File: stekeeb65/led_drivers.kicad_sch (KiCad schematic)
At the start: 28 parts

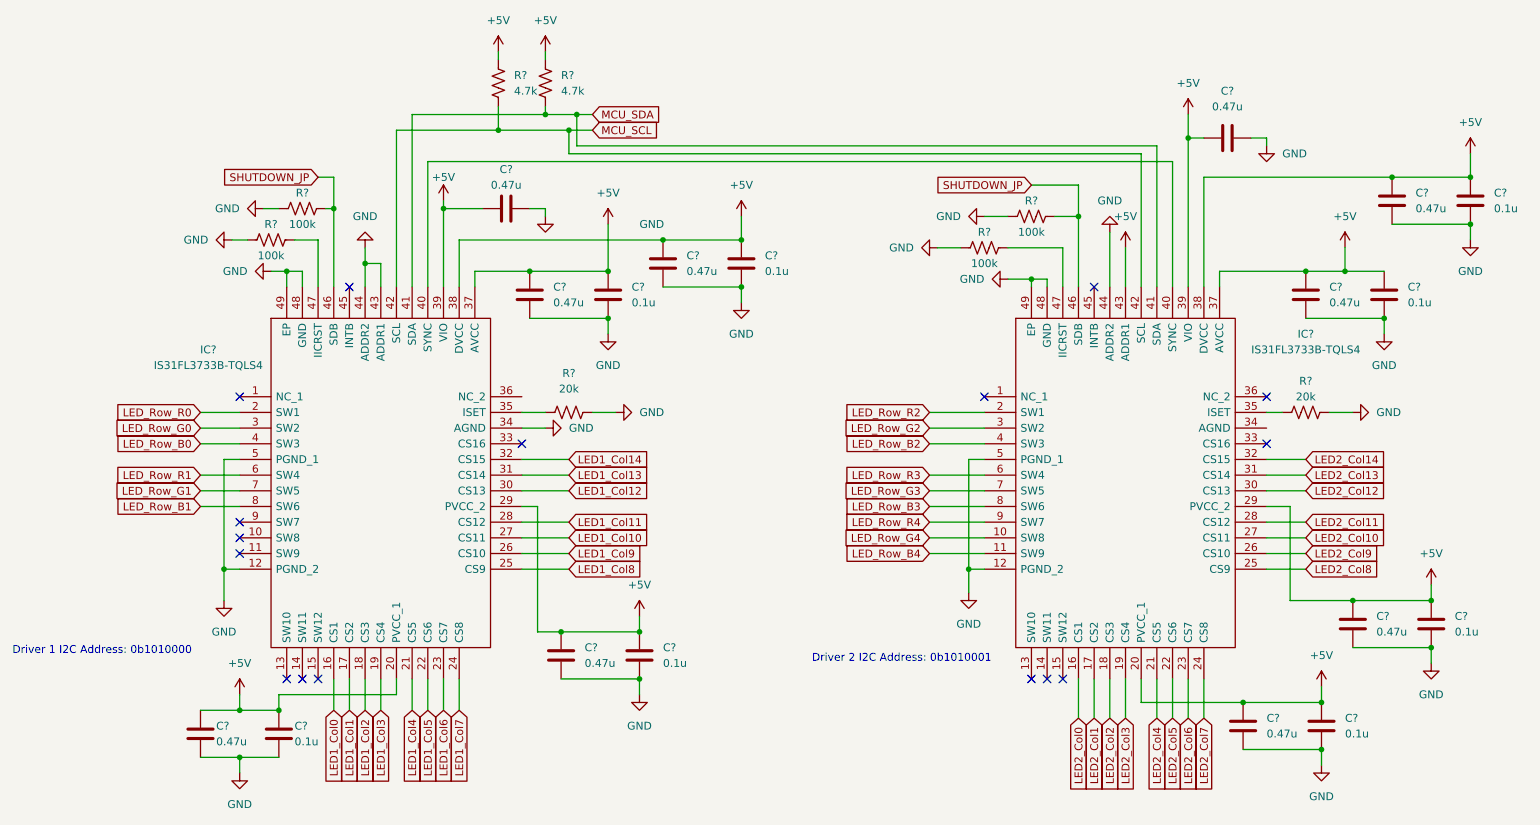
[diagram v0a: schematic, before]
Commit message: Adding keyboard footprints
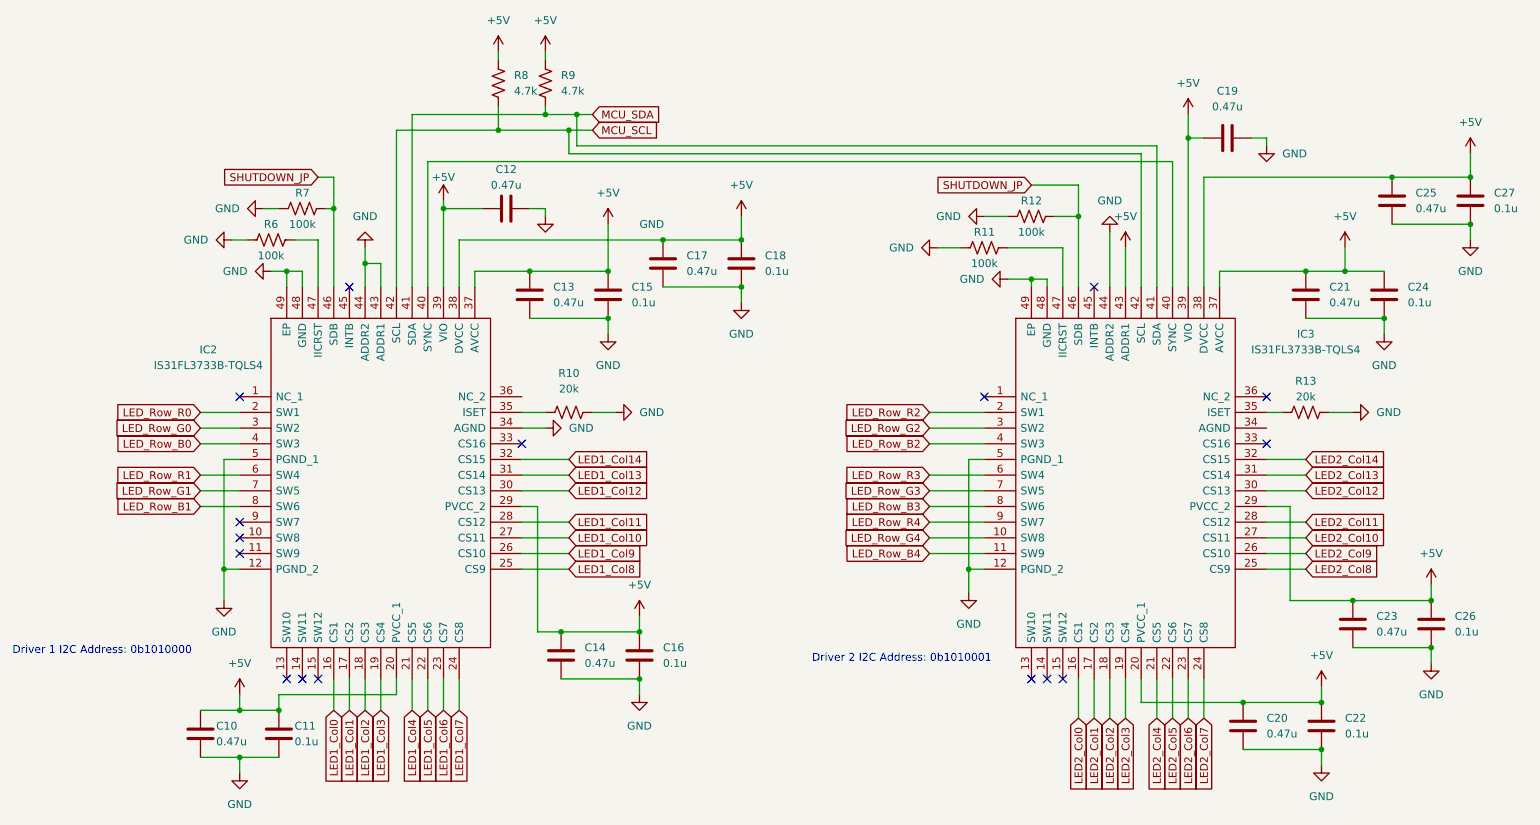
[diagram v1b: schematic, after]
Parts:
- C10, C11, C12, C13, C14, C15, C16, C17, C18, C19, C20, C21, C22, C23, C24, C25, C26, C27: renamed from C?; footprint (none) -> Capacitor_SMD:C_0805_2012Metric_Pad1.18x1.45mm_HandSolder
- R10, R11, R12, R13, R6, R7, R8, R9: renamed from R?; footprint (none) -> Resistor_SMD:R_0805_2012Metric_Pad1.20x1.40mm_HandSolder
- gave numbers to parts that had none: 2

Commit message: Adding key layout with leds
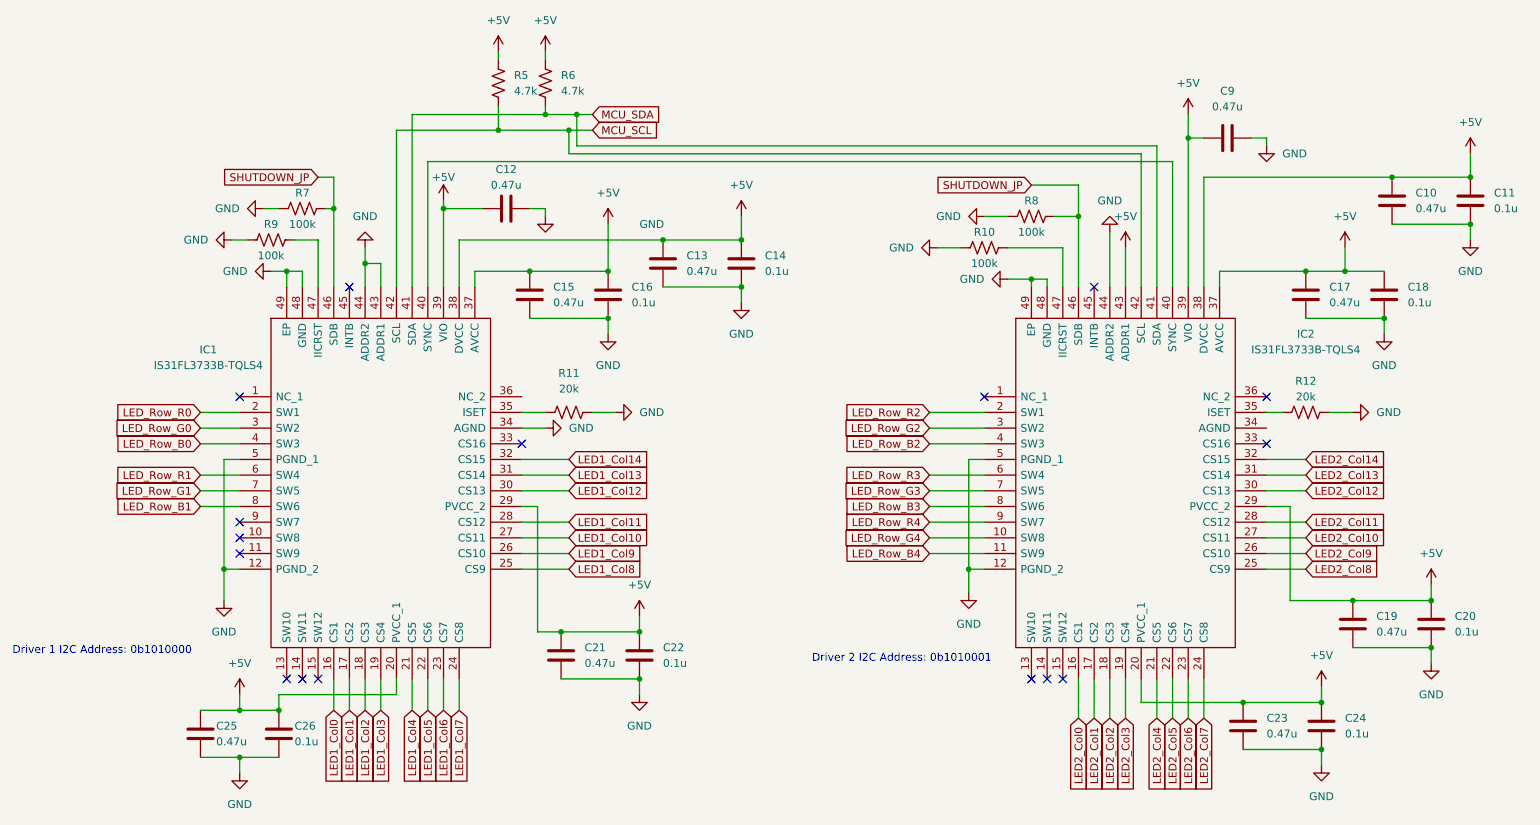
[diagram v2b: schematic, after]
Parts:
- renumbered C25 to C10, C27 to C11, C17 to C13, C18 to C14, C13 to C15, C15 to C16, C21 to C17, C24 to C18, C23 to C19, C26 to C20, C14 to C21, C16 to C22, C20 to C23, C22 to C24, C10 to C25, C11 to C26, C19 to C9, IC2 to IC1, IC3 to IC2, R11 to R10, R10 to R11, R13 to R12, R8 to R5, R9 to R6, R12 to R8, R6 to R9

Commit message: Adding layout for diodes, LEDs, edge cuts
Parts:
- IC1, IC2: footprint QFP50P900X900X120-49N -> SamacSys_Parts:QFP50P900X900X120-49N
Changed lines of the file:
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@@
     (property "Reference" "IC2" (id 0) (at 231.14 66.04 0))
     (property "Value" "IS31FL3733B-TQLS4" (id 1) (at 231.14 68.58 0))
-    (property "Footprint" "QFP50P900X900X120-49N" (id 2) (at 220.98 63.5 0)
+    (property "Footprint" "SamacSys_Parts:QFP50P900X900X120-49N" (id 2) (at 220.98 63.5 0)
       (effects (font (size 1.27 1.27)) (justify left) hide)
     )
@@
     (property "Reference" "IC1" (id 0) (at 53.34 68.58 0))
     (property "Value" "IS31FL3733B-TQLS4" (id 1) (at 53.34 71.12 0))
-    (property "Footprint" "QFP50P900X900X120-49N" (id 2) (at 100.33 63.5 0)
-      (effects (font (size 1.27 1.27)) (justify left) hide)
-    )
+    (property "Footprint" "SamacSys_Parts:QFP50P900X900X120-49N" (id 2) (at 100.33 63.5 0)
+      (effects (font (size 1.27 1.27)) (justify left) hide)
+    )

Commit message: Started layout for keyboard. still need to verify LED driver schematic
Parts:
- C10, C11, C12, C13, C14, C15, C16, C17, C18, C19, C20, C21, C22, C23, C24, C25, C26, C9: footprint Capacitor_SMD:C_0805_2012Metric_Pad1.18x1.45mm_HandSolder -> Capacitor_SMD:C_0603_1608Metric_Pad1.08x0.95mm_HandSolder
- R10, R11, R12, R5, R6, R7, R8, R9: footprint Resistor_SMD:R_0805_2012Metric_Pad1.20x1.40mm_HandSolder -> Resistor_SMD:R_0603_1608Metric_Pad0.98x0.95mm_HandSolder
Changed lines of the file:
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@@
       (effects (font (size 1.27 1.27)) (justify left))
     )
-    (property "Footprint" "Capacitor_SMD:C_0805_2012Metric_Pad1.18x1.45mm_HandSolder" (id 2) (at 252.4252 116.84 0)
+    (property "Footprint" "Capacitor_SMD:C_0603_1608Metric_Pad1.08x0.95mm_HandSolder" (id 2) (at 252.4252 116.84 0)
       (effects (font (size 1.27 1.27)) hide)
     )
@@
       (effects (font (size 1.27 1.27)) (justify left))
     )
-    (property "Footprint" "Capacitor_SMD:C_0805_2012Metric_Pad1.18x1.45mm_HandSolder" (id 2) (at 53.0352 134.62 0)
+    (property "Footprint" "Capacitor_SMD:C_0603_1608Metric_Pad1.08x0.95mm_HandSolder" (id 2) (at 53.0352 134.62 0)
       (effects (font (size 1.27 1.27)) hide)
     )
@@
       (effects (font (size 1.27 1.27)) (justify left))
     )
-    (property "Footprint" "Capacitor_SMD:C_0805_2012Metric_Pad1.18x1.45mm_HandSolder" (id 2) (at 119.0752 63.5 0)
+    (property "Footprint" "Capacitor_SMD:C_0603_1608Metric_Pad1.08x0.95mm_HandSolder" (id 2) (at 119.0752 63.5 0)
       (effects (font (size 1.27 1.27)) hide)
     )
@@
       (effects (font (size 1.27 1.27)) (justify left))
     )
-    (property "Footprint" "Capacitor_SMD:C_0805_2012Metric_Pad1.18x1.45mm_HandSolder" (id 2) (at 244.8052 63.5 0)
+    (property "Footprint" "Capacitor_SMD:C_0603_1608Metric_Pad1.08x0.95mm_HandSolder" (id 2) (at 244.8052 63.5 0)
       (effects (font (size 1.27 1.27)) hide)
     )
@@
     (property "Reference" "C9" (id 0) (at 218.44 26.67 90))
     (property "Value" "0.47u" (id 1) (at 218.44 29.21 90))
-    (property "Footprint" "Capacitor_SMD:C_0805_2012Metric_Pad1.18x1.45mm_HandSolder" (id 2) (at 222.25 33.3248 0)
+    (property "Footprint" "Capacitor_SMD:C_0603_1608Metric_Pad1.08x0.95mm_HandSolder" (id 2) (at 222.25 33.3248 0)
       (effects (font (size 1.27 1.27)) hide)
     )
@@
     (property "Reference" "R9" (id 0) (at 63.5 48.26 90))
     (property "Value" "100k" (id 1) (at 63.5 53.34 90))
-    (property "Footprint" "Resistor_SMD:R_0805_2012Metric_Pad1.20x1.40mm_HandSolder" (id 2) (at 63.754 49.784 90)
+    (property "Footprint" "Resistor_SMD:R_0603_1608Metric_Pad0.98x0.95mm_HandSolder" (id 2) (at 63.754 49.784 90)
       (effects (font (size 1.27 1.27)) hide)
     )
@@
       (effects (font (size 1.27 1.27)) (justify left))
     )
-    (property "Footprint" "Capacitor_SMD:C_0805_2012Metric_Pad1.18x1.45mm_HandSolder" (id 2) (at 111.4552 121.92 0)
+    (property "Footprint" "Capacitor_SMD:C_0603_1608Metric_Pad1.08x0.95mm_HandSolder" (id 2) (at 111.4552 121.92 0)
       (effects (font (size 1.27 1.27)) hide)
     )
@@
     (property "Reference" "C12" (id 0) (at 101.6 39.37 90))
     (property "Value" "0.47u" (id 1) (at 101.6 41.91 90))
-    (property "Footprint" "Capacitor_SMD:C_0805_2012Metric_Pad1.18x1.45mm_HandSolder" (id 2) (at 105.41 44.7548 0)
+    (property "Footprint" "Capacitor_SMD:C_0603_1608Metric_Pad1.08x0.95mm_HandSolder" (id 2) (at 105.41 44.7548 0)
       (effects (font (size 1.27 1.27)) hide)
     )
@@
       (effects (font (size 1.27 1.27)) (justify left))
     )
-    (property "Footprint" "Capacitor_SMD:C_0805_2012Metric_Pad1.18x1.45mm_HandSolder" (id 2) (at 127.9652 58.42 0)
+    (property "Footprint" "Capacitor_SMD:C_0603_1608Metric_Pad1.08x0.95mm_HandSolder" (id 2) (at 127.9652 58.42 0)
       (effects (font (size 1.27 1.27)) hide)
     )
@@
       (effects (font (size 1.27 1.27)) (justify left))
     )
-    (property "Footprint" "Capacitor_SMD:C_0805_2012Metric_Pad1.18x1.45mm_HandSolder" (id 2) (at 221.9452 133.35 0)
+    (property "Footprint" "Capacitor_SMD:C_0603_1608Metric_Pad1.08x0.95mm_HandSolder" (id 2) (at 221.9452 133.35 0)
       (effects (font (size 1.27 1.27)) hide)
     )
@@
       (effects (font (size 1.27 1.27)) (justify left))
     )
-    (property "Footprint" "Capacitor_SMD:C_0805_2012Metric_Pad1.18x1.45mm_HandSolder" (id 2) (at 124.1552 121.92 0)
+    (property "Footprint" "Capacitor_SMD:C_0603_1608Metric_Pad1.08x0.95mm_HandSolder" (id 2) (at 124.1552 121.92 0)
       (effects (font (size 1.27 1.27)) hide)
     )
@@
       (effects (font (size 1.27 1.27)) (justify left))
     )
-    (property "Footprint" "Capacitor_SMD:C_0805_2012Metric_Pad1.18x1.45mm_HandSolder" (id 2) (at 65.7352 134.62 0)
+    (property "Footprint" "Capacitor_SMD:C_0603_1608Metric_Pad1.08x0.95mm_HandSolder" (id 2) (at 65.7352 134.62 0)
       (effects (font (size 1.27 1.27)) hide)
     )
@@
       (effects (font (size 1.27 1.27)) (justify left))
     )
-    (property "Footprint" "Capacitor_SMD:C_0805_2012Metric_Pad1.18x1.45mm_HandSolder" (id 2) (at 140.6652 58.42 0)
+    (property "Footprint" "Capacitor_SMD:C_0603_1608Metric_Pad1.08x0.95mm_HandSolder" (id 2) (at 140.6652 58.42 0)
       (effects (font (size 1.27 1.27)) hide)
     )
@@
       (effects (font (size 1.27 1.27)) (justify left))
     )
-    (property "Footprint" "Capacitor_SMD:C_0805_2012Metric_Pad1.18x1.45mm_HandSolder" (id 2) (at 234.6452 133.35 0)
+    (property "Footprint" "Capacitor_SMD:C_0603_1608Metric_Pad1.08x0.95mm_HandSolder" (id 2) (at 234.6452 133.35 0)
       (effects (font (size 1.27 1.27)) hide)
     )
@@
     (property "Reference" "R8" (id 0) (at 186.69 44.45 90))
     (property "Value" "100k" (id 1) (at 186.69 49.53 90))
-    (property "Footprint" "Resistor_SMD:R_0805_2012Metric_Pad1.20x1.40mm_HandSolder" (id 2) (at 186.944 45.974 90)
+    (property "Footprint" "Resistor_SMD:R_0603_1608Metric_Pad0.98x0.95mm_HandSolder" (id 2) (at 186.944 45.974 90)
       (effects (font (size 1.27 1.27)) hide)
     )
@@
       (effects (font (size 1.27 1.27)) (justify left))
     )
-    (property "Footprint" "Capacitor_SMD:C_0805_2012Metric_Pad1.18x1.45mm_HandSolder" (id 2) (at 106.3752 63.5 0)
+    (property "Footprint" "Capacitor_SMD:C_0603_1608Metric_Pad1.08x0.95mm_HandSolder" (id 2) (at 106.3752 63.5 0)
       (effects (font (size 1.27 1.27)) hide)
     )
@@
       (effects (font (size 1.27 1.27)) (justify left))
     )
-    (property "Footprint" "Resistor_SMD:R_0805_2012Metric_Pad1.20x1.40mm_HandSolder" (id 2) (at 101.346 25.654 90)
+    (property "Footprint" "Resistor_SMD:R_0603_1608Metric_Pad0.98x0.95mm_HandSolder" (id 2) (at 101.346 25.654 90)
       (effects (font (size 1.27 1.27)) hide)
     )
@@
       (effects (font (size 1.27 1.27)) (justify left))
     )
-    (property "Footprint" "Capacitor_SMD:C_0805_2012Metric_Pad1.18x1.45mm_HandSolder" (id 2) (at 239.7252 116.84 0)
+    (property "Footprint" "Capacitor_SMD:C_0603_1608Metric_Pad1.08x0.95mm_HandSolder" (id 2) (at 239.7252 116.84 0)
       (effects (font (size 1.27 1.27)) hide)
     )
@@
     (property "Reference" "R7" (id 0) (at 68.58 43.18 90))
     (property "Value" "100k" (id 1) (at 68.58 48.26 90))
-    (property "Footprint" "Resistor_SMD:R_0805_2012Metric_Pad1.20x1.40mm_HandSolder" (id 2) (at 68.834 44.704 90)
+    (property "Footprint" "Resistor_SMD:R_0603_1608Metric_Pad0.98x0.95mm_HandSolder" (id 2) (at 68.834 44.704 90)
       (effects (font (size 1.27 1.27)) hide)
     )
@@
     (property "Reference" "R12" (id 0) (at 231.14 73.66 90))
     (property "Value" "20k" (id 1) (at 231.14 76.2 90))
-    (property "Footprint" "Resistor_SMD:R_0805_2012Metric_Pad1.20x1.40mm_HandSolder" (id 2) (at 231.394 77.724 90)
+    (property "Footprint" "Resistor_SMD:R_0603_1608Metric_Pad0.98x0.95mm_HandSolder" (id 2) (at 231.394 77.724 90)
       (effects (font (size 1.27 1.27)) hide)
     )
@@
     (property "Reference" "R11" (id 0) (at 111.76 72.39 90))
     (property "Value" "20k" (id 1) (at 111.76 74.93 90))
-    (property "Footprint" "Resistor_SMD:R_0805_2012Metric_Pad1.20x1.40mm_HandSolder" (id 2) (at 112.014 77.724 90)
+    (property "Footprint" "Resistor_SMD:R_0603_1608Metric_Pad0.98x0.95mm_HandSolder" (id 2) (at 112.014 77.724 90)
       (effects (font (size 1.27 1.27)) hide)
     )
@@
       (effects (font (size 1.27 1.27)) (justify left))
     )
-    (property "Footprint" "Capacitor_SMD:C_0805_2012Metric_Pad1.18x1.45mm_HandSolder" (id 2) (at 232.1052 63.5 0)
+    (property "Footprint" "Capacitor_SMD:C_0603_1608Metric_Pad1.08x0.95mm_HandSolder" (id 2) (at 232.1052 63.5 0)
       (effects (font (size 1.27 1.27)) hide)
     )
@@
     (property "Reference" "R10" (id 0) (at 179.07 49.53 90))
     (property "Value" "100k" (id 1) (at 179.07 54.61 90))
-    (property "Footprint" "Resistor_SMD:R_0805_2012Metric_Pad1.20x1.40mm_HandSolder" (id 2) (at 179.324 51.054 90)
+    (property "Footprint" "Resistor_SMD:R_0603_1608Metric_Pad0.98x0.95mm_HandSolder" (id 2) (at 179.324 51.054 90)
       (effects (font (size 1.27 1.27)) hide)
     )
@@
       (effects (font (size 1.27 1.27)) (justify left))
     )
-    (property "Footprint" "Capacitor_SMD:C_0805_2012Metric_Pad1.18x1.45mm_HandSolder" (id 2) (at 258.7752 48.26 0)
+    (property "Footprint" "Capacitor_SMD:C_0603_1608Metric_Pad1.08x0.95mm_HandSolder" (id 2) (at 258.7752 48.26 0)
       (effects (font (size 1.27 1.27)) hide)
     )
@@
       (effects (font (size 1.27 1.27)) (justify left))
     )
-    (property "Footprint" "Resistor_SMD:R_0805_2012Metric_Pad1.20x1.40mm_HandSolder" (id 2) (at 108.966 25.654 90)
+    (property "Footprint" "Resistor_SMD:R_0603_1608Metric_Pad0.98x0.95mm_HandSolder" (id 2) (at 108.966 25.654 90)
       (effects (font (size 1.27 1.27)) hide)
     )
@@
       (effects (font (size 1.27 1.27)) (justify left))
     )
-    (property "Footprint" "Capacitor_SMD:C_0805_2012Metric_Pad1.18x1.45mm_HandSolder" (id 2) (at 246.0752 48.26 0)
-      (effects (font (size 1.27 1.27)) hide)
-    )
+    (property "Footprint" "Capacitor_SMD:C_0603_1608Metric_Pad1.08x0.95mm_HandSolder" (id 2) (at 246.0752 48.26 0)
+      (effects (font (size 1.27 1.27)) hide)
+    )
